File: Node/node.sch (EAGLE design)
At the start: 96 parts, among them CN4 MicroUSB, J1 U.FL, U1 MCP73871, U2 DW1000-I, U3 TPS61090RSAR, U4 ATMEGA328, X2 332-02, Y1 8MHz

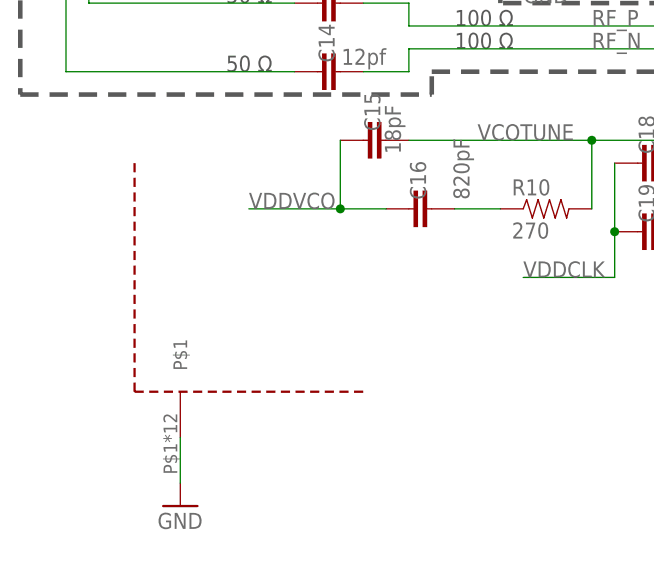
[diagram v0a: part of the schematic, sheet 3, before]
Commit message: More RF work. Increased the RF shield size, routed TCXO.
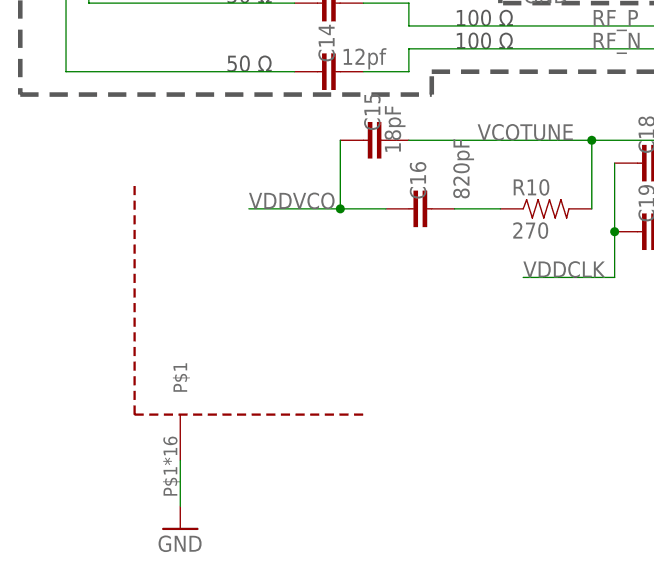
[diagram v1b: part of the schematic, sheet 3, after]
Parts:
- removed U$1: 5BMI-S-202-F, MainLib:5BMI-S-202-F
- added U$6: SMS-255F, MainLib:SMS-255F
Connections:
- net GND: now also U$6.P$1; no longer U$1.P$1
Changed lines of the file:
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@@
 <part name="C31" library="SparkFun-Passives" deviceset="CAP" device="0402-CAP" value="22uF"/>
 <part name="L2" library="Wurth_Elektronik_Passive_rev15e" deviceset="WE-CBA" device="_0402(HC)" value="BLM15AG601SN1D"/>
-<part name="U$1" library="MainLib" deviceset="5BMI-S-202-F" device=""/>
-<part name="GND16" library="SparkFun-Aesthetics" deviceset="GND" device=""/>
 <part name="SJ1" library="jumper" library_urn="urn:adsk.eagle:library:252" deviceset="SJ" device="" package3d_urn="urn:adsk.eagle:package:15471/1"/>
 <part name="TX" library="SparkFun-LED" deviceset="LED" device="0603"/>
@@
 <part name="U$15" library="microbuilder" deviceset="VBAT" device=""/>
 <part name="L4" library="MainLib" deviceset="DR73-6R8-R" device="" value="https://www.digikey.com/product-detail/en/eaton-electronics-division/DR73-6R8-R/513-1134-1-ND/754632"/>
-<part name="GND19" library="supply1" deviceset="GND" device=""/>
+<part name="GND19" library="supply1" library_urn="urn:adsk.eagle:library:371" deviceset="GND" device=""/>
 <part name="R13" library="SparkFun-Passives" deviceset="RESISTOR" device="0805-RES" value="270K"/>
 <part name="R14" library="SparkFun-Passives" deviceset="RESISTOR" device="0805-RES" value="100K"/>
-<part name="GND20" library="supply1" deviceset="GND" device=""/>
+<part name="GND20" library="supply1" library_urn="urn:adsk.eagle:library:371" deviceset="GND" device=""/>
 <part name="DONE" library="microbuilder" deviceset="LED" device="0805_NOOUTLINE" value="GREEN"/>
 <part name="CHRG/LBO" library="microbuilder" deviceset="LED" device="0805_NOOUTLINE" value="ORANGE"/>
@@
 <part name="R16" library="SparkFun-Passives" deviceset="RESISTOR" device="0805-RES" value="1K"/>
 <part name="C17" library="SparkFun-Passives" deviceset="CAP" device="0805" value="10uF"/>
-<part name="GND21" library="supply1" deviceset="GND" device=""/>
+<part name="GND21" library="supply1" library_urn="urn:adsk.eagle:library:371" deviceset="GND" device=""/>
 <part name="R17" library="SparkFun-Passives" deviceset="RESISTOR" device="0805-RES" value="2.0K"/>
 <part name="R20" library="SparkFun-Passives" deviceset="RESISTOR" device="0805-RES" value="100K"/>
-<part name="GND22" library="supply1" deviceset="GND" device=""/>
-<part name="GND23" library="supply1" deviceset="GND" device=""/>
-<part name="GND24" library="supply1" deviceset="GND" device=""/>
+<part name="GND22" library="supply1" library_urn="urn:adsk.eagle:library:371" deviceset="GND" device=""/>
+<part name="GND23" library="supply1" library_urn="urn:adsk.eagle:library:371" deviceset="GND" device=""/>
+<part name="GND24" library="supply1" library_urn="urn:adsk.eagle:library:371" deviceset="GND" device=""/>
 <part name="THERM" library="SparkFun-Passives" deviceset="RESISTOR" device="0805-RES" value="15K"/>
 <part name="U$2" library="microbuilder" deviceset="VBAT" device=""/>
@@
 <part name="C6" library="SparkFun-Passives" deviceset="CAP" device="0805" value="10uF"/>
 <part name="CN4" library="microbuilder" deviceset="USB" device="MICRO_20329" value="MicroUSB"/>
-<part name="GND25" library="supply1" deviceset="GND" device=""/>
-<part name="GND26" library="supply1" deviceset="GND" device=""/>
+<part name="GND25" library="supply1" library_urn="urn:adsk.eagle:library:371" deviceset="GND" device=""/>
+<part name="GND26" library="supply1" library_urn="urn:adsk.eagle:library:371" deviceset="GND" device=""/>
 <part name="U$4" library="microbuilder" deviceset="VBUS" device=""/>
+<part name="U$6" library="MainLib" deviceset="SMS-255F" device=""/>
+<part name="GND27" library="SparkFun-Aesthetics" deviceset="GND" device=""/>
 </parts>
 <sheets>
@@
 <attribute name="NAME" x="314.96" y="76.2" size="1.778" layer="95"/>
 </instance>
-<instance part="U$1" gate="G$1" x="38.1" y="33.02" smashed="yes"/>
-<instance part="GND16" gate="1" x="38.1" y="15.24" smashed="yes">
-<attribute name="VALUE" x="35.56" y="12.7" size="1.778" layer="96"/>
-</instance>
 <instance part="TX" gate="G$1" x="187.96" y="43.18" smashed="yes">
 <attribute name="NAME" x="191.516" y="38.608" size="1.778" layer="95" rot="R90"/>
@@
 <attribute name="NAME" x="81.153" y="116.586" size="1.778" layer="95" rot="R270"/>
 <attribute name="VALUE" x="84.455" y="126.492" size="1.778" layer="96" rot="R270"/>
+</instance>
+<instance part="U$6" gate="G$1" x="38.1" y="30.48" smashed="yes"/>
+<instance part="GND27" gate="1" x="38.1" y="12.7" smashed="yes">
+<attribute name="VALUE" x="35.56" y="10.16" size="1.778" layer="96"/>
 </instance>
 </instances>
@@
 <wire x1="330.2" y1="81.28" x2="335.28" y2="81.28" width="0.1524" layer="91"/>
 <junction x="330.2" y="81.28"/>
-</segment>
-<segment>
-<pinref part="GND16" gate="1" pin="GND"/>
-<pinref part="U$1" gate="G$1" pin="P$1"/>
-<wire x1="38.1" y1="22.86" x2="38.1" y2="17.78" width="0.1524" layer="91"/>
 </segment>
 <segment>
@@
 <junction x="96.52" y="111.76"/>
 </segment>
-</net>
+<segment>
+<pinref part="U$6" gate="G$1" pin="P$1"/>
+<wire x1="38.1" y1="20.32" x2="38.1" y2="15.24" width="0.1524" layer="91"/>
+<pinref part="GND27" gate="1" pin="GND"/>
+</segment>
+</net>

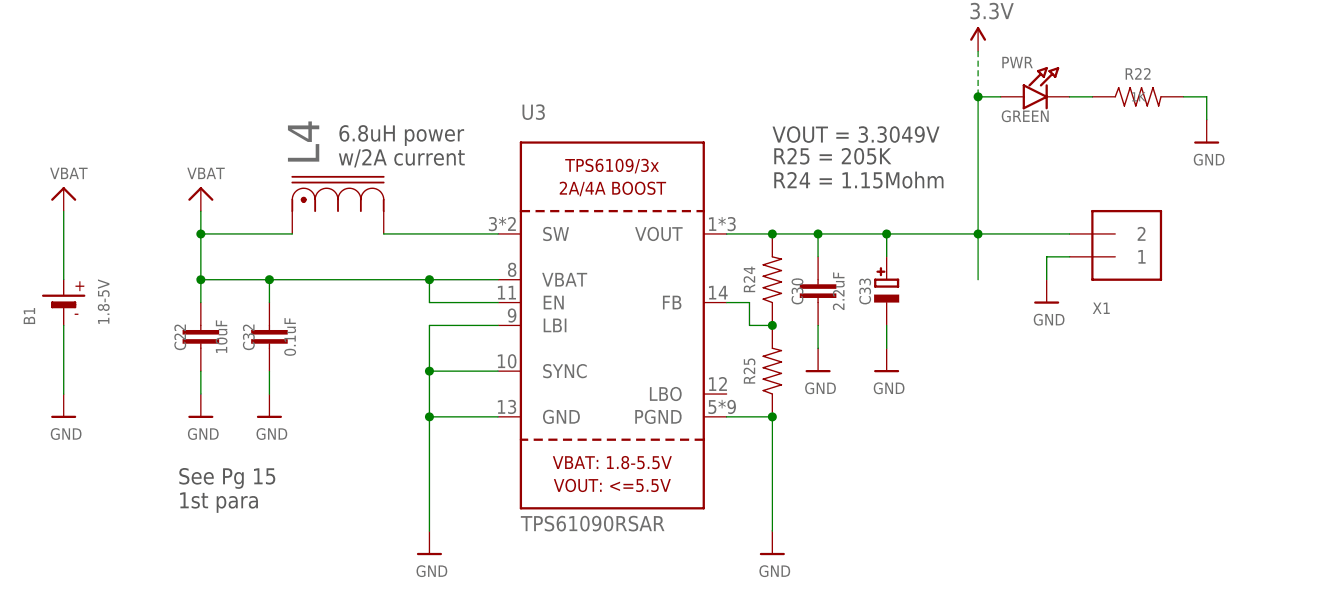
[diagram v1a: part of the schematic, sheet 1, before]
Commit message: Removed unneeded JST connector
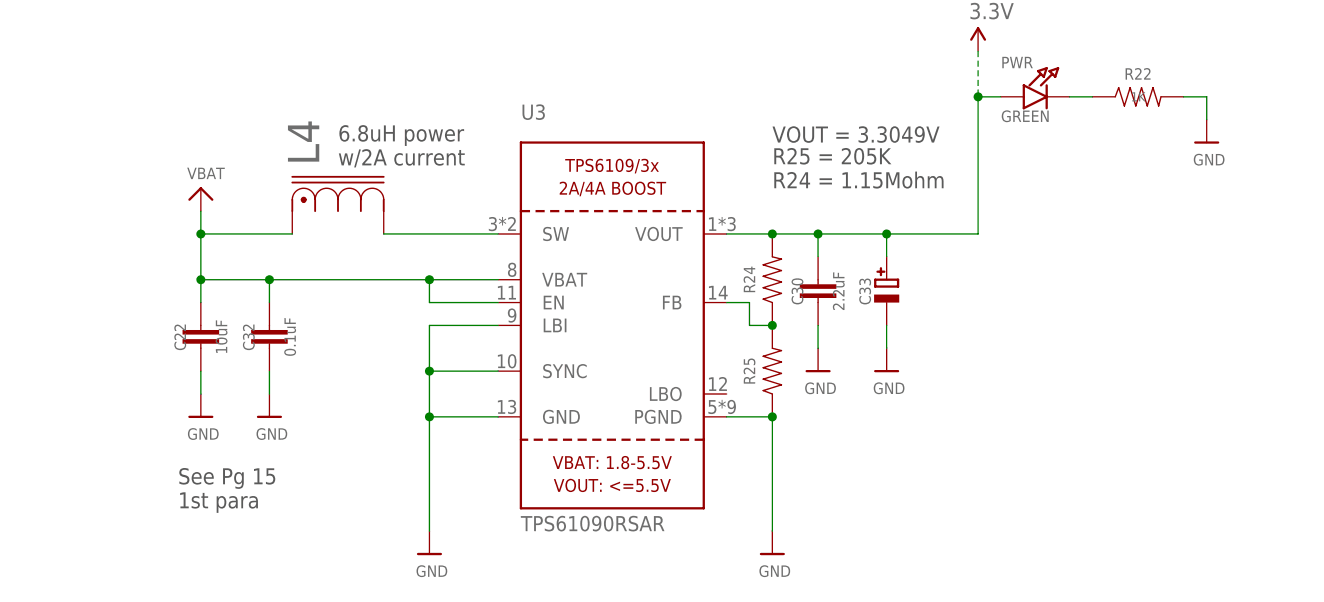
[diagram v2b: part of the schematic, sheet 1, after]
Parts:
- removed B1: 1.8-5V, microbuilder:BATTERY
- removed X1: (no value), microbuilder:TERMBLOCK_1X2
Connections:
- net 3.3V: no longer X1.2
- net GND: no longer B1.-, X1.1
- net VBAT: no longer B1.+
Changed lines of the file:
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@@
 <part name="C22" library="SparkFun-Passives" deviceset="CAP" device="0805" value="10uF"/>
 <part name="U$19" library="microbuilder" deviceset="GND" device=""/>
-<part name="B1" library="microbuilder" deviceset="BATTERY" device="" value="1.8-5V"/>
-<part name="U$23" library="microbuilder" deviceset="GND" device=""/>
 <part name="C30" library="SparkFun-Passives" deviceset="CAP" device="0805" value="2.2uF"/>
-<part name="X1" library="microbuilder" deviceset="TERMBLOCK_1X2" device=""/>
 <part name="U$28" library="microbuilder" deviceset="VBAT" device=""/>
 <part name="PWR" library="microbuilder" deviceset="LED" device="0805_NOOUTLINE" value="GREEN"/>
@@
 <part name="U$32" library="microbuilder" deviceset="GND" device=""/>
 <part name="U$33" library="microbuilder" deviceset="GND" device=""/>
-<part name="U$34" library="microbuilder" deviceset="GND" device=""/>
 <part name="U$35" library="microbuilder" deviceset="GND" device=""/>
 <part name="C33" library="microbuilder" deviceset="CAP_TANTALUM" device="B/3528_REFLOW" value="100uF/6V - https://www.digikey.com/product-detail/en/avx-corporation/F930G107MBA/478-8135-1-ND/4005827"/>
 <part name="SUPPLY9" library="SparkFun-Aesthetics" deviceset="3.3V" device=""/>
 <part name="U$13" library="microbuilder" deviceset="GND" device=""/>
-<part name="U$15" library="microbuilder" deviceset="VBAT" device=""/>
 <part name="L4" library="MainLib" deviceset="DR73-6R8-R" device="" value="https://www.digikey.com/product-detail/en/eaton-electronics-division/DR73-6R8-R/513-1134-1-ND/754632"/>
 <part name="GND19" library="supply1" library_urn="urn:adsk.eagle:library:371" deviceset="GND" device=""/>
@@
 <attribute name="VALUE" x="28.956" y="45.72" size="1.27" layer="96"/>
 </instance>
-<instance part="B1" gate="G$1" x="15.24" y="60.96" smashed="yes" rot="R90">
-<attribute name="NAME" x="12.065" y="58.42" size="1.27" layer="95" rot="R90"/>
-<attribute name="VALUE" x="20.32" y="58.42" size="1.27" layer="96" rot="R90"/>
-</instance>
-<instance part="U$23" gate="G$1" x="15.24" y="48.26" smashed="yes">
-<attribute name="VALUE" x="13.716" y="45.72" size="1.27" layer="96"/>
-</instance>
 <instance part="C30" gate="G$1" x="99.06" y="60.96" smashed="yes">
 <attribute name="NAME" x="96.77" y="62.21" size="1.27" layer="95" font="vector" rot="R90" align="center"/>
 <attribute name="VALUE" x="101.36" y="62.21" size="1.27" layer="96" font="vector" rot="R90" align="center"/>
 </instance>
-<instance part="X1" gate="G$1" x="132.08" y="68.58" smashed="yes" rot="MR180">
-<attribute name="VALUE" x="129.54" y="73.66" size="1.27" layer="96" rot="MR180"/>
-<attribute name="NAME" x="129.54" y="60.96" size="1.27" layer="95" rot="MR180"/>
-</instance>
 <instance part="U$28" gate="G$1" x="30.48" y="73.66" smashed="yes">
 <attribute name="VALUE" x="28.956" y="74.676" size="1.27" layer="96"/>
@@
 <attribute name="VALUE" x="105.156" y="50.8" size="1.27" layer="96"/>
 </instance>
-<instance part="U$34" gate="G$1" x="124.46" y="60.96" smashed="yes">
-<attribute name="VALUE" x="122.936" y="58.42" size="1.27" layer="96"/>
-</instance>
 <instance part="U$35" gate="G$1" x="142.24" y="78.74" smashed="yes">
 <attribute name="VALUE" x="140.716" y="76.2" size="1.27" layer="96"/>
@@
 <instance part="U$13" gate="G$1" x="66.04" y="137.16" smashed="yes">
 <attribute name="VALUE" x="64.516" y="134.62" size="1.27" layer="96"/>
-</instance>
-<instance part="U$15" gate="G$1" x="15.24" y="73.66" smashed="yes">
-<attribute name="VALUE" x="13.716" y="74.676" size="1.27" layer="96"/>
 </instance>
 <instance part="L4" gate="A" x="40.64" y="68.58" smashed="yes" rot="R90">
@@
 </segment>
 <segment>
-<pinref part="B1" gate="G$1" pin="-"/>
-<pinref part="U$23" gate="G$1" pin="GND"/>
-<wire x1="15.24" y1="58.42" x2="15.24" y2="50.8" width="0.1524" layer="91"/>
-</segment>
-<segment>
 <pinref part="U$30" gate="G$1" pin="GND"/>
 <pinref part="C32" gate="G$1" pin="2"/>
@@
 <pinref part="U$33" gate="G$1" pin="GND"/>
 <pinref part="C33" gate="G$1" pin="-"/>
-</segment>
-<segment>
-<wire x1="124.46" y1="66.04" x2="124.46" y2="63.5" width="0.1524" layer="91"/>
-<pinref part="X1" gate="G$1" pin="1"/>
-<wire x1="124.46" y1="66.04" x2="127" y2="66.04" width="0.1524" layer="91"/>
-<pinref part="U$34" gate="G$1" pin="GND"/>
 </segment>
 <segment>
@@
 </segment>
 <segment>
-<pinref part="B1" gate="G$1" pin="+"/>
-<wire x1="15.24" y1="71.12" x2="15.24" y2="63.5" width="0.1524" layer="91"/>
-<pinref part="U$15" gate="G$1" pin="VBAT"/>
-</segment>
-<segment>
 <pinref part="U$2" gate="G$1" pin="VBAT"/>
 <wire x1="243.84" y1="142.24" x2="243.84" y2="137.16" width="0.1524" layer="91"/>
@@
 <wire x1="99.06" y1="66.04" x2="99.06" y2="68.58" width="0.1524" layer="91"/>
 <junction x="99.06" y="68.58"/>
-<junction x="116.84" y="68.58"/>
 <pinref part="PWR" gate="G$1" pin="A"/>
 <wire x1="119.38" y1="83.82" x2="116.84" y2="83.82" width="0.1524" layer="91"/>
 <wire x1="106.68" y1="68.58" x2="106.68" y2="66.04" width="0.1524" layer="91"/>
 <junction x="106.68" y="68.58"/>
-<pinref part="X1" gate="G$1" pin="2"/>
-<wire x1="127" y1="68.58" x2="116.84" y2="68.58" width="0.1524" layer="91"/>
 <pinref part="R24" gate="G$1" pin="2"/>
 <junction x="93.98" y="68.58"/>
@@
 <wire x1="116.84" y1="88.9" x2="116.84" y2="83.82" width="0.1524" layer="91" style="longdash"/>
 <junction x="116.84" y="83.82"/>
-<wire x1="116.84" y1="68.58" x2="116.84" y2="63.5" width="0.1524" layer="91"/>
-</segment>
-</net>
+</segment>
+</net>
